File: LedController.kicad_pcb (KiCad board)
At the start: 2 copper layers, 4 parts, among them P1 CONN_7

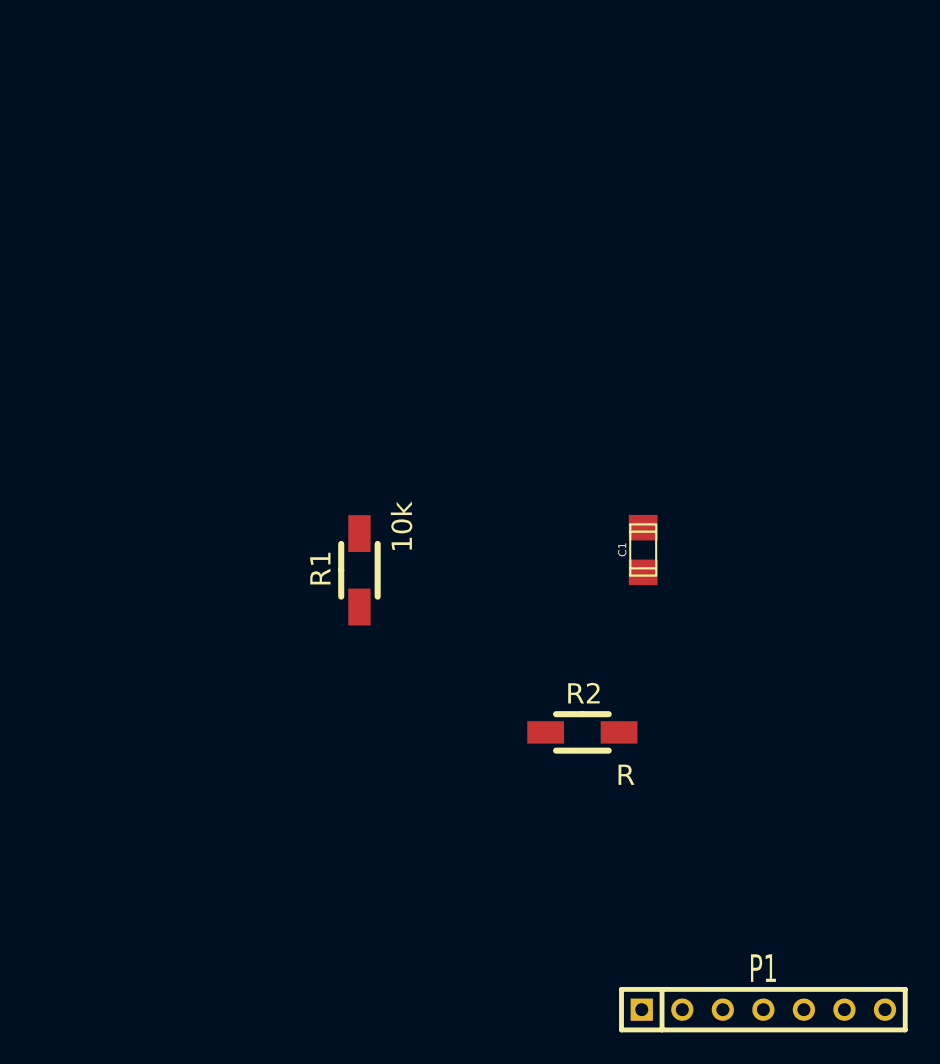
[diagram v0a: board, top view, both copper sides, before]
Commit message: Added FET footprint and did inital board placement
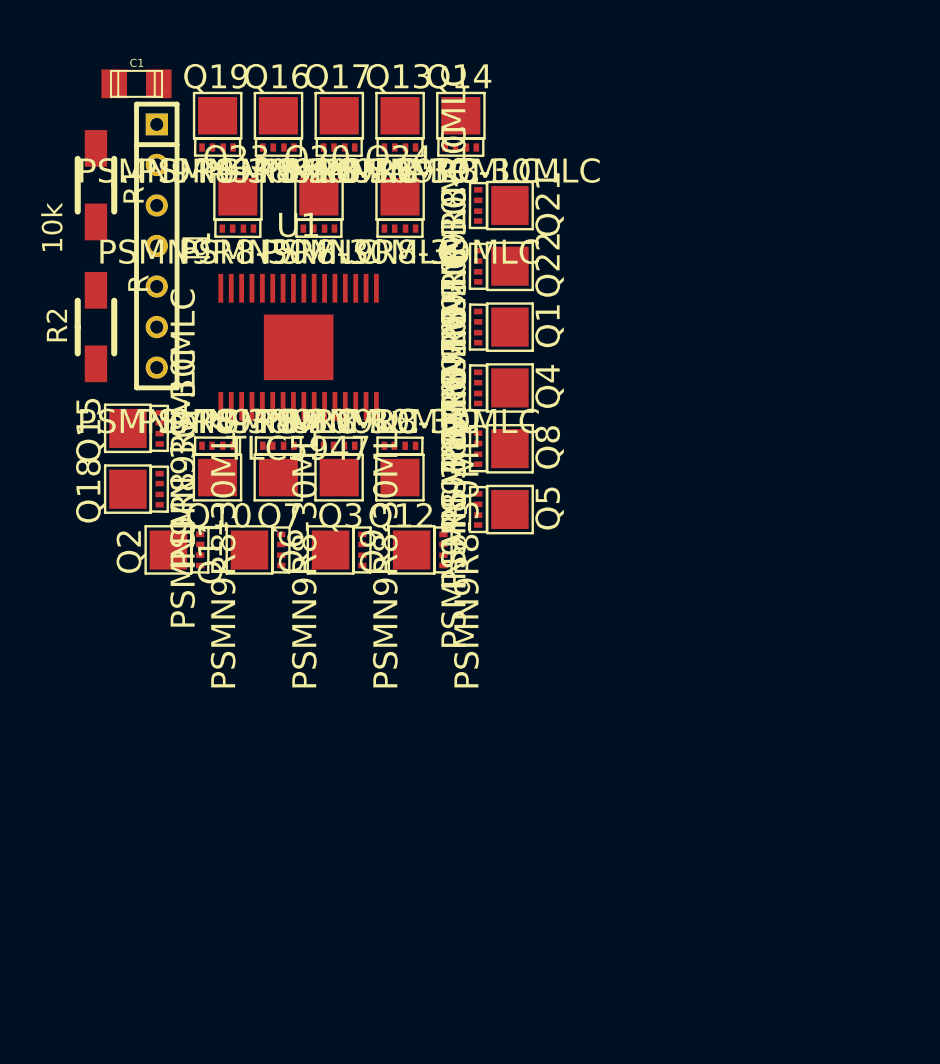
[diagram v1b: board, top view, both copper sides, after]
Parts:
- added Q1: PSMN9R8-30MLC, LedController:PSMN9R8-30MLC, F.Cu at (132.1, 62.2)
- added Q10: PSMN9R8-30MLC, LedController:PSMN9R8-30MLC, F.Cu at (114.3, 71.1)
- added Q11: PSMN9R8-30MLC, LedController:PSMN9R8-30MLC, F.Cu at (116.8, 76.2)
- added Q12: PSMN9R8-30MLC, LedController:PSMN9R8-30MLC, F.Cu at (125.7, 71.1)
- added Q13: PSMN9R8-30MLC, LedController:PSMN9R8-30MLC, F.Cu at (125.7, 49.5)
- added Q14: PSMN9R8-30MLC, LedController:PSMN9R8-30MLC, F.Cu at (129.5, 49.5)
- added Q15: PSMN9R8-30MLC, LedController:PSMN9R8-30MLC, F.Cu at (109.2, 68.6)
- added Q16: PSMN9R8-30MLC, LedController:PSMN9R8-30MLC, F.Cu at (118.1, 49.5)
- added Q17: PSMN9R8-30MLC, LedController:PSMN9R8-30MLC, F.Cu at (121.9, 49.5)
- added Q18: PSMN9R8-30MLC, LedController:PSMN9R8-30MLC, F.Cu at (109.2, 72.4)
- added Q19: PSMN9R8-30MLC, LedController:PSMN9R8-30MLC, F.Cu at (114.3, 49.5)
- added Q2: PSMN9R8-30MLC, LedController:PSMN9R8-30MLC, F.Cu at (111.8, 76.2)
- added Q20: PSMN9R8-30MLC, LedController:PSMN9R8-30MLC, F.Cu at (120.7, 54.6)
- added Q21: PSMN9R8-30MLC, LedController:PSMN9R8-30MLC, F.Cu at (132.1, 54.6)
- added Q22: PSMN9R8-30MLC, LedController:PSMN9R8-30MLC, F.Cu at (132.1, 58.4)
- added Q23: PSMN9R8-30MLC, LedController:PSMN9R8-30MLC, F.Cu at (115.6, 54.6)
- added Q24: PSMN9R8-30MLC, LedController:PSMN9R8-30MLC, F.Cu at (125.7, 54.6)
- added Q3: PSMN9R8-30MLC, LedController:PSMN9R8-30MLC, F.Cu at (121.9, 71.1)
- added Q4: PSMN9R8-30MLC, LedController:PSMN9R8-30MLC, F.Cu at (132.1, 66.0)
- added Q5: PSMN9R8-30MLC, LedController:PSMN9R8-30MLC, F.Cu at (132.1, 73.7)
- added Q6: PSMN9R8-30MLC, LedController:PSMN9R8-30MLC, F.Cu at (121.9, 76.2)
- added Q7: PSMN9R8-30MLC, LedController:PSMN9R8-30MLC, F.Cu at (118.1, 71.1)
- added Q8: PSMN9R8-30MLC, LedController:PSMN9R8-30MLC, F.Cu at (132.1, 69.8)
- added Q9: PSMN9R8-30MLC, LedController:PSMN9R8-30MLC, F.Cu at (127.0, 76.2)
- added U1: TLC5947, LedController:tlc5947, F.Cu at (119.4, 63.5)
- moved P1 61.1 mm to (110.5, 57.1), turned to 270 degrees
- moved C1 43.1 mm to (109.2, 47.0), turned to 0 degrees
- moved R2 39.7 mm to (106.7, 62.2), turned to 90 degrees
- moved R1 29.2 mm to (106.7, 53.3), turned to 270 degrees
